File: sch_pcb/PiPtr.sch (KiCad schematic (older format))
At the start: 51 parts, among them J101 GLOBAL_LINK_LEFT, J102 GLOBAL_LINK_RIGHT, J103 RTC, J107 RASPBERRY_PI, J111 FP_PIXEL, J112 AM2302, J113 I2C1_5V, J117 OLED_SSD1306, Q101 BSS138, Q102 BSS138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

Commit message: Add files via upload
Remove OLED connector
Remove extra bypass cap from third EEPOT
More routing - got the soundcards and usb hub done.  Only remaining big section is the DC-DC.  Still a bit of pain-in-the-tuchas traces that need to sneak across the board...
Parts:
- removed C110: 0.1u, lib:smd0603, symbol C
- removed J117: OLED_SSD1306, lib:SIL-4, symbol CONN_01X04
- J103: footprint (none) -> lib:SIL-5
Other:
- note removed: "Address: 0x3C"
- note removed: "Caution: Watch power polarity"
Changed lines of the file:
@@
 Text Label 2100 3875 2    60   ~ 0
 UINTB_33
-$Comp
-L C C110
-U 1 1 5968C303
-P 7050 6275
-F 0 "C110" H 7075 6375 50  0000 L CNN
-F 1 "0.1u" H 7075 6175 50  0000 L CNN
-F 2 "lib:smd0603" H 7088 6125 50  0001 C CNN
-F 3 "" H 7050 6275 50  0001 C CNN
-	1    7050 6275
-	1    0    0    -1
-$EndComp
 Text Label 6100 6825 2    60   ~ 0
 MISO_33
@@
 	5225 6300 5775 6300
 Wire Wire Line
-	7050 6025 7050 6125
-Wire Wire Line
-	6725 6025 6725 6125
-Connection ~ 6725 6025
-Wire Wire Line
 	6400 6125 6400 6025
 Connection ~ 6400 6025
 Wire Wire Line
 	6400 6425 6400 6525
-Wire Wire Line
-	6400 6475 7050 6475
-Wire Wire Line
-	7050 6475 7050 6425
 Connection ~ 6400 6475
-Wire Wire Line
-	6725 6425 6725 6475
-Connection ~ 6725 6475
 Wire Wire Line
 	4225 6100 4225 6200
@@
 $EndComp
 $Comp
-L CONN_01X04 J117
-U 1 1 595CF549
-P 10225 3700
-F 0 "J117" H 10175 3950 50  0000 C CNN
-F 1 "OLED_SSD1306" V 10325 3700 50  0000 C CNN
-F 2 "lib:SIL-4" H 10225 3700 50  0001 C CNN
-F 3 "" H 10225 3700 50  0001 C CNN
-	1    10225 3700
-	1    0    0    -1
-$EndComp
-Wire Wire Line
-	10025 3750 9425 3750
-Wire Wire Line
-	10025 3850 9425 3850
-Text Label 9425 3850 0    60   ~ 0
-SDA1_33
-Text Label 9425 3750 0    60   ~ 0
-SCL1_33
-Wire Wire Line
-	10025 3550 9950 3550
-Wire Wire Line
-	9950 3550 9950 3900
-Wire Wire Line
-	10025 3650 9875 3650
-Wire Wire Line
-	9875 3650 9875 3475
-$Comp
-L GND #PWR040
-U 1 1 595D2DC1
-P 9950 3900
-F 0 "#PWR040" H 9950 3650 50  0001 C CNN
-F 1 "GND" H 9950 3750 50  0001 C CNN
-F 2 "" H 9950 3900 50  0001 C CNN
-F 3 "" H 9950 3900 50  0001 C CNN
-	1    9950 3900
-	1    0    0    -1
-$EndComp
-$Comp
-L +3.3V #PWR041
-U 1 1 595D34C7
-P 9875 3475
-F 0 "#PWR041" H 9875 3325 50  0001 C CNN
-F 1 "+3.3V" H 9875 3615 50  0000 C CNN
-F 2 "" H 9875 3475 50  0001 C CNN
-F 3 "" H 9875 3475 50  0001 C CNN
-	1    9875 3475
-	1    0    0    -1
-$EndComp
-Text Notes 9275 4225 0    50   ~ 0
-Caution: Watch power polarity
-$Comp
 L TESTPOINT TP102
 U 1 1 595D9A4E
@@
 	1    0    0    -1
 $EndComp
-Text Notes 9825 4125 0    60   ~ 0
-Address: 0x3C
 Text Notes 2875 3175 0    60   ~ 0
 Address 0x21
@@
 Connection ~ 3850 5750
 Wire Wire Line
-	5350 6025 7050 6025
+	5350 6025 6725 6025
 Text Label 7875 3025 0    60   ~ 0
 PIXEL_33
@@
 F 0 "J103" H 10200 5300 50  0000 C CNN
 F 1 "RTC" V 10300 5000 50  0000 C CNN
-F 2 "" H 10200 4950 50  0001 C CNN
+F 2 "lib:SIL-5" H 10200 4950 50  0001 C CNN
 F 3 "" H 10200 4950 50  0001 C CNN
 	1    10200 5000
@@
 Text Notes 9350 5500 0    60   ~ 0
 For optional RTC board
+Wire Wire Line
+	6725 6025 6725 6125
+Wire Wire Line
+	6725 6425 6725 6475
+Wire Wire Line
+	6725 6475 6400 6475
 $EndSCHEMATC

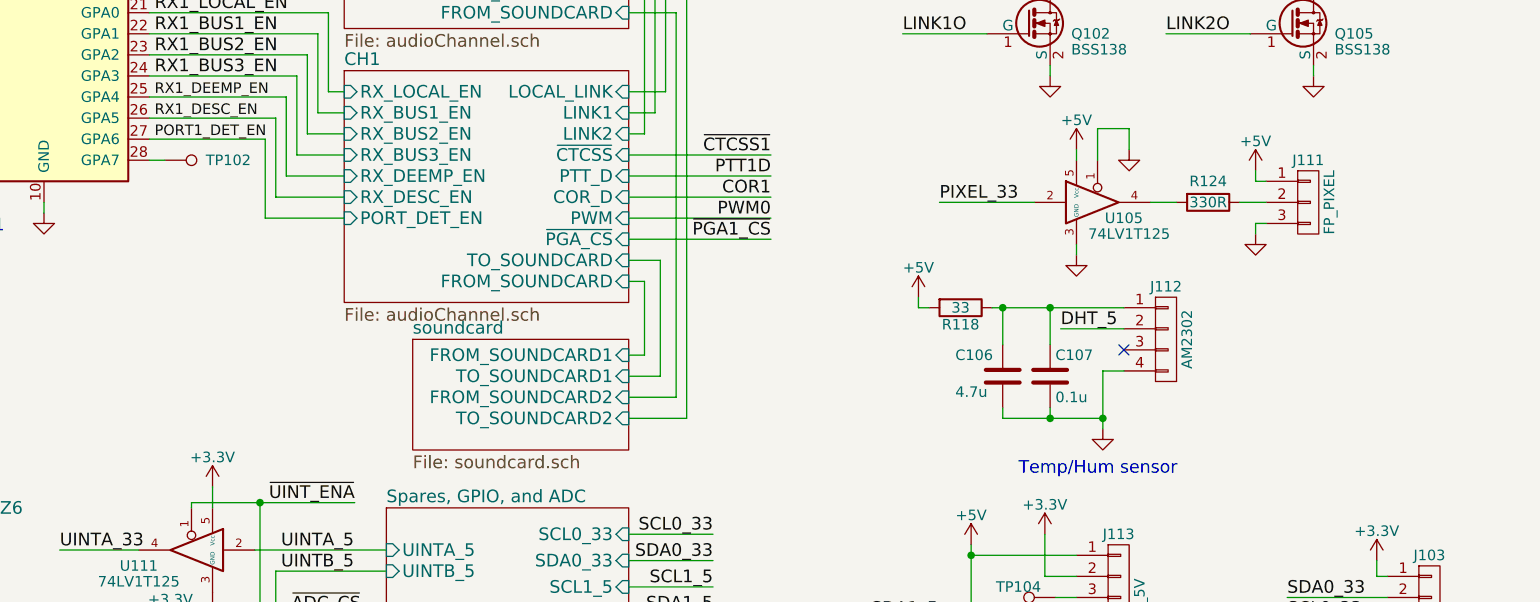
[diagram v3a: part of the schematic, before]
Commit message: Add files via upload
Add a PMOS switch to allow turning on the soundcard section (hub and 2 soundcard chips) after the Pi has booted.  For some reason, doing so before the desktop loads causes it to hang..
Change gain resistors in opamp stages to move the sweet spot closer to the center of the digital pots to allow for more adjustment range
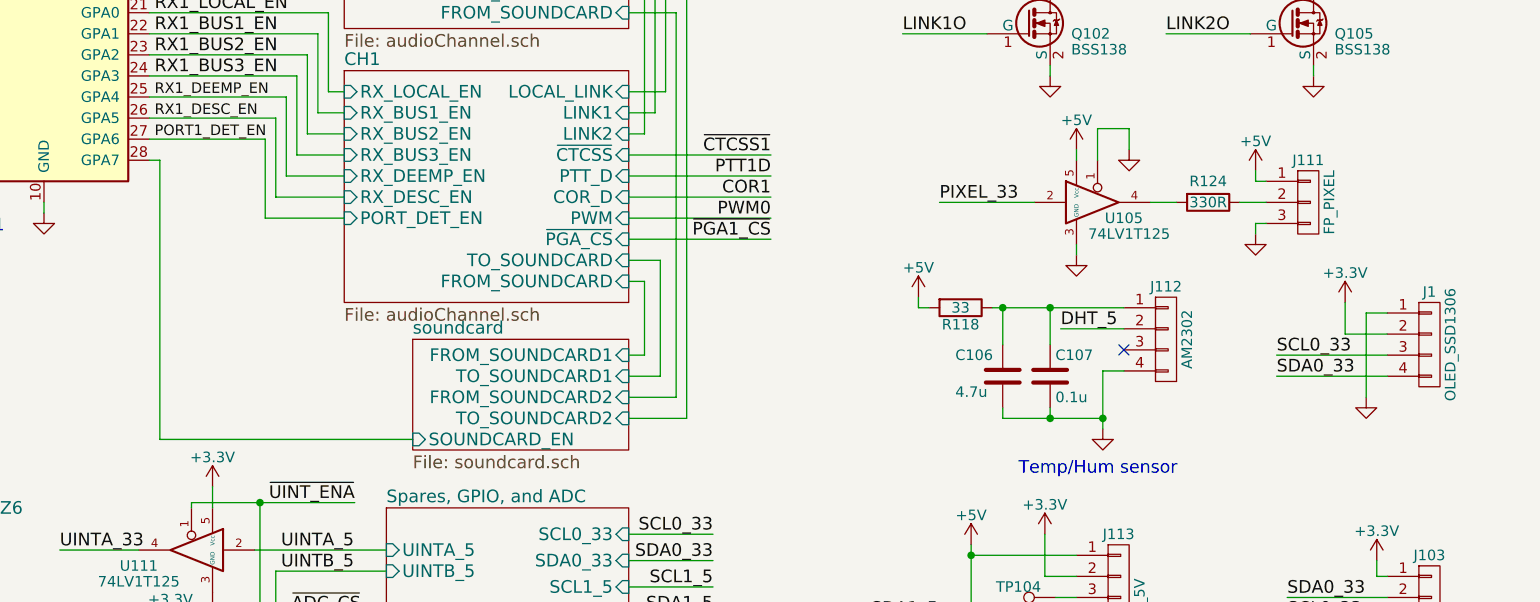
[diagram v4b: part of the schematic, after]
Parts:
- removed TP102: TESTPOINT, lib:Wire_28AWG, symbol TESTPOINT
- added J1: OLED_SSD1306, lib:SIL-4, symbol CONN_01X04
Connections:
- net +3V3: now also J1.2 (P2)
- net GND: now also J1.1 (P1)
- net SCL0_33: now also J1.3 (P3)
- net SDA0_33: now also J1.4 (P4)
- net soundcard/SOUNDCARD_EN: now reaches U101.28 (GPA7)
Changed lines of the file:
@@
 EESchema Schematic File Version 2
 LIBS:PiPtr
-LIBS:conn
+LIBS:power
 LIBS:PiPtr-cache
 EELAYER 26 0
@@
 F4 "FROM_SOUNDCARD2" I R 6400 3950 60
 F5 "TO_SOUNDCARD2" I R 6400 4050 60
+F6 "SOUNDCARD_EN" I L 5375 4150 60
 $EndSheet
 $Comp
@@
 Wire Wire Line
 	4675 3100 5050 3100
-Wire Wire Line
-	4125 2825 4200 2825
 Wire Wire Line
 	6400 1225 6575 1225
@@
 $EndComp
 $Comp
-L TESTPOINT TP102
-U 1 1 595D9A4E
-P 4200 2825
-F 0 "TP102" H 4500 2825 50  0000 C CNN
-F 1 "TESTPOINT" H 4600 2900 60  0001 C CNN
-F 2 "lib:Wire_28AWG" H 4200 2825 60  0001 C CNN
-F 3 "" H 4200 2825 60  0000 C CNN
-	1    4200 2825
-	1    0    0    -1
-$EndComp
-$Comp
 L TESTPOINT TP103
 U 1 1 595DBEF8
@@
 Wire Wire Line
 	6725 6475 6400 6475
+$Comp
+L CONN_01X04 J1
+U 1 1 599B67A3
+P 10200 3700
+F 0 "J1" H 10200 3950 50  0000 C CNN
+F 1 "OLED_SSD1306" V 10300 3700 50  0000 C CNN
+F 2 "lib:SIL-4" H 10200 3700 50  0001 C CNN
+F 3 "" H 10200 3700 50  0001 C CNN
+	1    10200 3700
+	1    0    0    -1
+$EndComp
+$Comp
+L GND #PWR059
+U 1 1 599B82B1
+P 9900 3950
+F 0 "#PWR059" H 9900 3700 50  0001 C CNN
+F 1 "GND" H 9900 3800 50  0001 C CNN
+F 2 "" H 9900 3950 50  0001 C CNN
+F 3 "" H 9900 3950 50  0001 C CNN
+	1    9900 3950
+	1    0    0    -1
+$EndComp
+$Comp
+L +3.3V #PWR060
+U 1 1 599B842E
+P 9800 3500
+F 0 "#PWR060" H 9800 3350 50  0001 C CNN
+F 1 "+3.3V" H 9800 3640 50  0000 C CNN
+F 2 "" H 9800 3500 50  0001 C CNN
+F 3 "" H 9800 3500 50  0001 C CNN
+	1    9800 3500
+	1    0    0    -1
+$EndComp
+Wire Wire Line
+	10000 3750 9475 3750
+Wire Wire Line
+	10000 3850 9475 3850
+Wire Wire Line
+	9900 3550 9900 3950
+Wire Wire Line
+	9900 3550 10000 3550
+Wire Wire Line
+	10000 3650 9800 3650
+Wire Wire Line
+	9800 3650 9800 3500
+Text Label 9475 3750 0    60   ~ 0
+SCL0_33
+Text Label 9475 3850 0    60   ~ 0
+SDA0_33
+Wire Wire Line
+	4125 2825 4175 2825
+Wire Wire Line
+	4175 2825 4175 4150
+Wire Wire Line
+	4175 4150 5375 4150
 $EndSCHEMATC

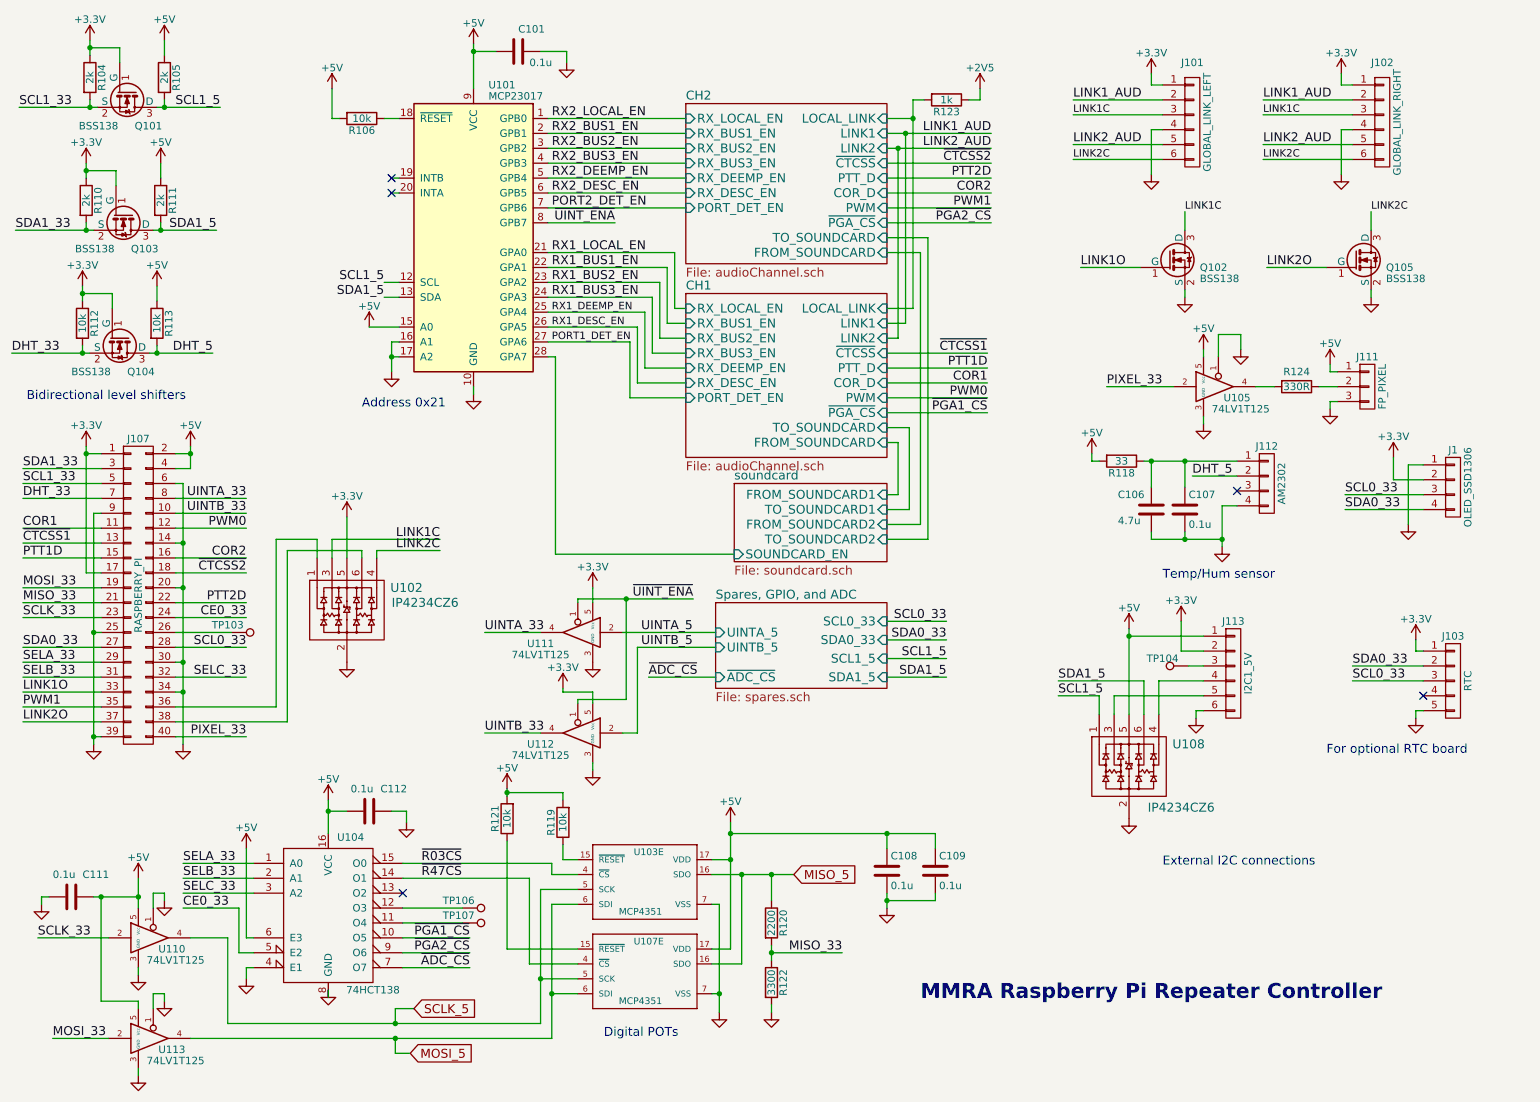
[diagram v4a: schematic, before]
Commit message: Update board with third soundcard
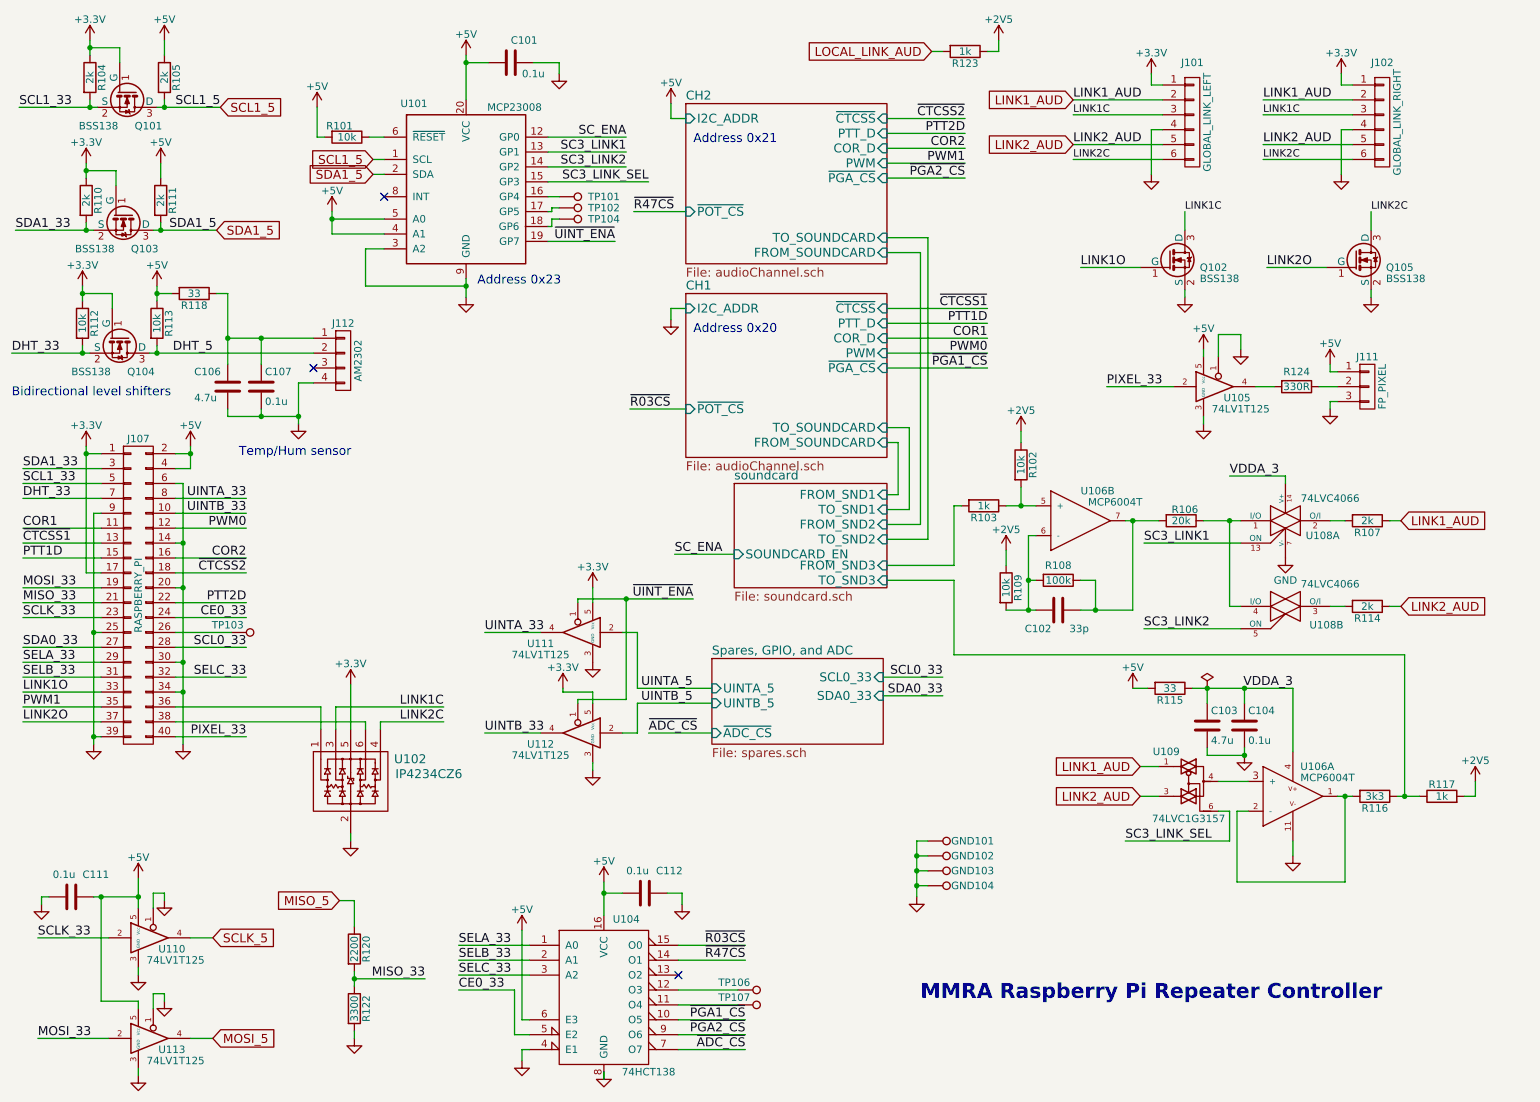
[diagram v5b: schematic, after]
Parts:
- removed C108, C109: 0.1u, lib:smd0603, symbol C
- removed J1: OLED_SSD1306, lib:SIL-4, symbol CONN_01X04
- removed J103: RTC, lib:SIL-5, symbol CONN_01X05
- removed J113: I2C1_5V, lib:SIL-6, symbol CONN_01X06
- removed R119, R121: 10k, lib:smd0603, symbol R
- removed U101: MCP23017, lib:SOIC28, symbol MCP23017
- removed U103, U107: MCP4351, lib:SSOP-20, symbol MCP344XD
- removed U108: IP4234CZ6, lib:SOT23-6, symbol IP4234CZ6_USB_ESD_PROTECTOR
- added C102: 33p, lib:smd0603, symbol C
- added C103: 4.7u, lib:smd0603, symbol C
- added C104: 0.1u, lib:smd0603, symbol C
- added GND101, GND102, GND103, GND104, TP101, TP102: TESTPOINT, lib:Wire_28AWG, symbol TESTPOINT
- added R101, R102, R109: 10k, lib:smd0603, symbol R
- added R103, R117: 1k, lib:smd0603, symbol R
- added R107, R114: 2k, lib:smd0603, symbol R
- added R108: 100k, lib:smd0603, symbol R
- added R115: 33, lib:smd0603, symbol R
- added R116: 3k3, lib:smd0603, symbol R
- added U101: MCP23008, lib:SSOP-20, symbol MCP23008_SSOP20
- added U106: MCP6004T, lib:SOIC14, symbol MCP6004N
- added U108: 74LVC4066, lib:SOIC14, symbol 74LVC4066
- added U109: 74LVC1G3157, lib:SOT23-6, symbol 74LVC1G3157
- R106: value 10k -> 20k
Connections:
- net +2V5: now also R102.1, R109.1, R117.2
- net +5V: now also R101.2, R115.2, U101.20 (VCC), U101.4 (A1), U101.5 (A0); no longer R106.2
- net GND: now also C103.2, C104.2, GND101.1, GND102.1, GND103.1, GND104.1, U101.3 (A2), U101.9 (GND), U106.11 (V-), U108.7 (V-), U109.2 (GND)
- net LINK1_AUD: now also R107.1, U109.1
- net LINK2_AUD: now also R114.1, U109.3
- net SCL1_5: now also U101.1 (SCL)
- net SDA1_5: now also U101.2 (SDA)
- net ~UINT_ENA: now also U101.19 (GP7)
- net at TP104.1: now also U101.18 (GP6)
- net at R106.1: now also U108.1 (I/O), U108.4 (I/O)
- net CH1/LOCAL_LINK renamed LOCAL_LINK_AUD
- new net: R102.2, R103.1, U106.5 (+)
- new net: C102.2, R108.2, R109.2, U106.6 (-)
- new net: C102.1, R106.2, R108.1, U106.7 (OUT)
- new net: R107.2, U108.2 (O/I)
- new net: R114.2, U108.3 (O/I)
- new net: R116.2, U106.1 (OUT), U106.2 (-)
- new net: U106.3 (+), U109.4
- new net: TP101.1, U101.16 (GP4)
- new net: TP102.1, U101.17 (GP5)
- new net: R101.1, U101.6 (~RESET)
- new net SC3_LINK1: U101.13 (GP1), U108.13 (ON)
- new net SC3_LINK2: U101.14 (GP2), U108.5 (ON)
- new net SC3_LINK_SEL: U101.15 (GP3), U109.6
- new net SC_ENA: U101.12 (GP0)
- new net VCC: U109.5 (VCC)
- new net VDDA_3: C103.1, C104.1, R115.1, U106.4 (V+), U108.14 (V+)
- new net soundcard/FROM_SND3: R103.2
- new net soundcard/TO_SND3: R116.1, R117.1
- no-connect marks 5 -> 3
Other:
- note added: "Address 0x20"
- note added: "Address 0x23"
- note removed: "Digital POTs"
- note removed: "External I2C connections"
- note removed: "For optional RTC board"
- moved on the sheet: C106, C107, C112, J112, R118, R120, R122, R123, TP106, TP107, U102, U104

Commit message: BOM scrub
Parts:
- R120: value 2200 -> 2k2
- R122: value 3300 -> 3k3
- R124: value 330R -> 100
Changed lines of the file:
@@
 P 2825 6800
 F 0 "R120" V 2905 6800 50  0000 C CNN
-F 1 "2200" V 2825 6800 50  0000 C CNN
+F 1 "2k2" V 2825 6800 50  0000 C CNN
 F 2 "lib:smd0603" V 2755 6800 50  0001 C CNN
 F 3 "" H 2825 6800 50  0001 C CNN
@@
 P 2825 7200
 F 0 "R122" V 2905 7200 50  0000 C CNN
-F 1 "3300" V 2825 7200 50  0000 C CNN
+F 1 "3k3" V 2825 7200 50  0000 C CNN
 F 2 "lib:smd0603" V 2755 7200 50  0001 C CNN
 F 3 "" H 2825 7200 50  0001 C CNN
@@
 P 9150 3025
 F 0 "R124" V 9050 3025 50  0000 C CNN
-F 1 "330R" V 9150 3025 50  0000 C CNN
+F 1 "100" V 9150 3025 50  0000 C CNN
 F 2 "lib:smd0603" V 9080 3025 50  0001 C CNN
 F 3 "" H 9150 3025 50  0001 C CNN

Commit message: Move link connector close to edge to allow using jumpers to connect boards
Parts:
- J101, J102: footprint lib:Molex_22-27-2061_100mil_6pin_verical -> lib:SIL-6
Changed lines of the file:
@@
 F 0 "J101" H 8450 1650 50  0000 C CNN
 F 1 "GLOBAL_LINK_LEFT" V 8550 1250 50  0000 C CNN
-F 2 "lib:Molex_22-27-2061_100mil_6pin_verical" H 8450 1250 50  0001 C CNN
+F 2 "lib:SIL-6" H 8450 1250 50  0001 C CNN
 F 3 "" H 8450 1250 50  0001 C CNN
 	1    8450 1250
@@
 F 0 "J102" H 9725 1650 50  0000 C CNN
 F 1 "GLOBAL_LINK_RIGHT" V 9825 1250 50  0000 C CNN
-F 2 "lib:Molex_22-27-2061_100mil_6pin_verical" H 9725 1250 50  0001 C CNN
+F 2 "lib:SIL-6" H 9725 1250 50  0001 C CNN
 F 3 "" H 9725 1250 50  0001 C CNN
 	1    9725 1250
